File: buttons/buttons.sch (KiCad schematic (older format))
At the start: 20 parts, among them SW1 SW_Push, SW2 SW_Push, SW3 SW_Push, SW4 SW_Push, SW5 SW_Push, SW6 SW_Push, SW7 SW_Push, SW8 SW_Push

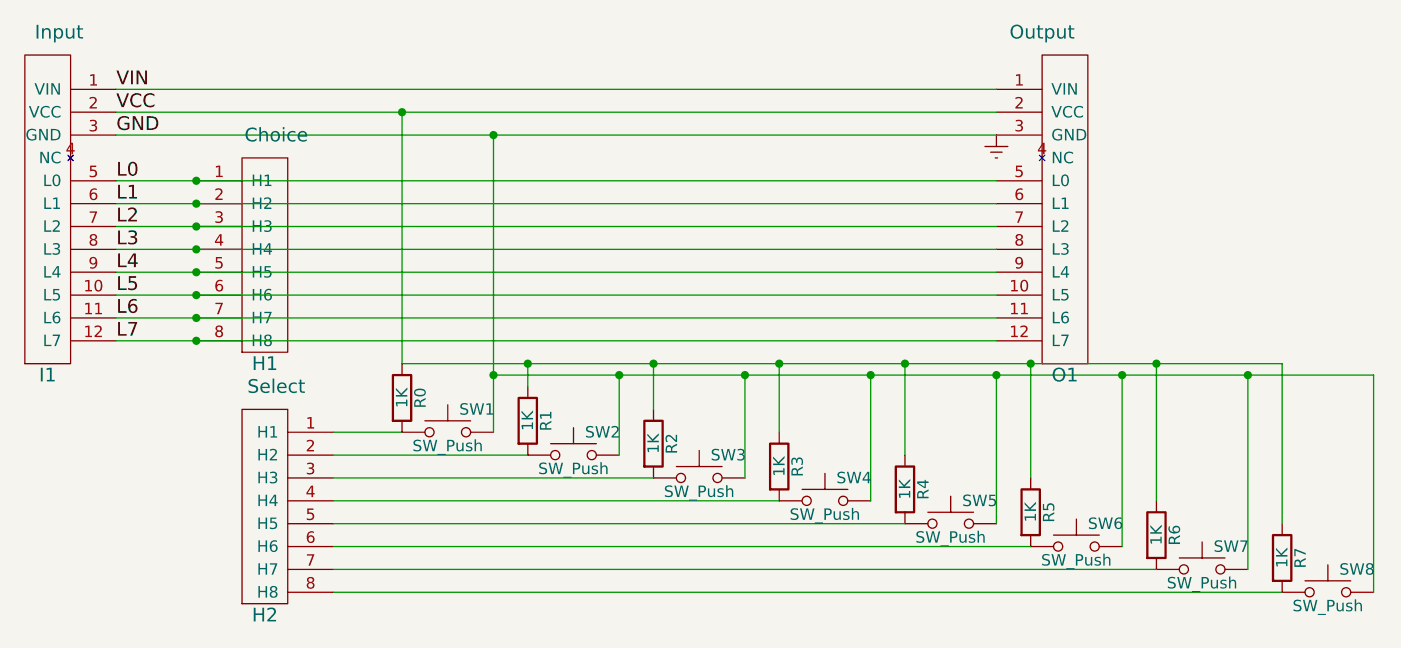
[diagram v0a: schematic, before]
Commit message: More work to ensure there are no errors from KiCAD's schematic checker. Fixed the multiplexer module, so that all 7 slaves will work (only 6 were working, due to a missing VCC to the "Next Output").
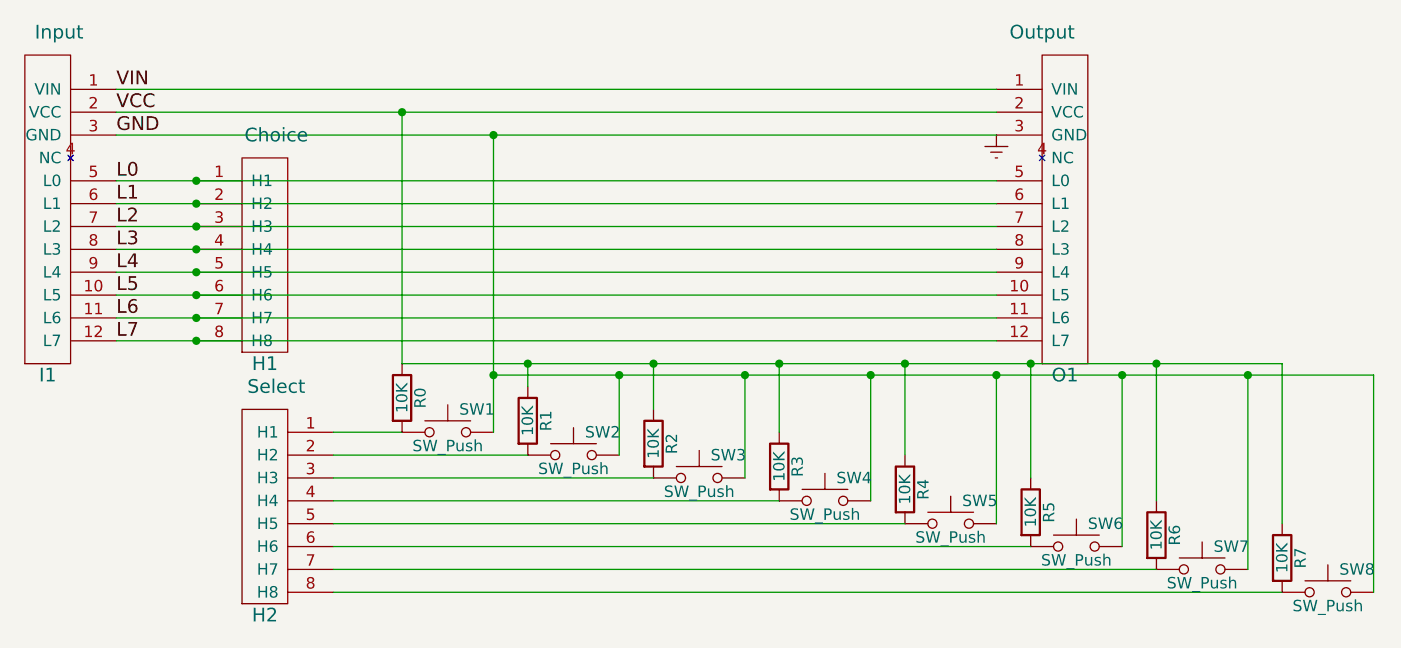
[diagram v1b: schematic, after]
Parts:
- R0, R1, R2, R3, R4, R5, R6, R7: value 1K -> 10K
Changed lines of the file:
@@
 LIBS:valves
 LIBS:eplay
-LIBS:Switch
-LIBS:buttons-cache
 EELAYER 25 0
 EELAYER END
@@
 P 3500 3250
 F 0 "R0" V 3580 3250 50  0000 C CNN
-F 1 "1K" V 3500 3250 50  0000 C CNN
+F 1 "10K" V 3500 3250 50  0000 C CNN
 F 2 "Resistors_THT:R_Axial_DIN0204_L3.6mm_D1.6mm_P7.62mm_Horizontal" V 3430 3250 50  0001 C CNN
 F 3 "" H 3500 3250 50  0001 C CNN
@@
 P 4050 3350
 F 0 "R1" V 4130 3350 50  0000 C CNN
-F 1 "1K" V 4050 3350 50  0000 C CNN
+F 1 "10K" V 4050 3350 50  0000 C CNN
 F 2 "Resistors_THT:R_Axial_DIN0204_L3.6mm_D1.6mm_P7.62mm_Horizontal" V 3980 3350 50  0001 C CNN
 F 3 "" H 4050 3350 50  0001 C CNN
@@
 P 4600 3450
 F 0 "R2" V 4680 3450 50  0000 C CNN
-F 1 "1K" V 4600 3450 50  0000 C CNN
+F 1 "10K" V 4600 3450 50  0000 C CNN
 F 2 "Resistors_THT:R_Axial_DIN0204_L3.6mm_D1.6mm_P7.62mm_Horizontal" V 4530 3450 50  0001 C CNN
 F 3 "" H 4600 3450 50  0001 C CNN
@@
 P 5150 3550
 F 0 "R3" V 5230 3550 50  0000 C CNN
-F 1 "1K" V 5150 3550 50  0000 C CNN
+F 1 "10K" V 5150 3550 50  0000 C CNN
 F 2 "Resistors_THT:R_Axial_DIN0204_L3.6mm_D1.6mm_P7.62mm_Horizontal" V 5080 3550 50  0001 C CNN
 F 3 "" H 5150 3550 50  0001 C CNN
@@
 P 5700 3650
 F 0 "R4" V 5780 3650 50  0000 C CNN
-F 1 "1K" V 5700 3650 50  0000 C CNN
+F 1 "10K" V 5700 3650 50  0000 C CNN
 F 2 "Resistors_THT:R_Axial_DIN0204_L3.6mm_D1.6mm_P7.62mm_Horizontal" V 5630 3650 50  0001 C CNN
 F 3 "" H 5700 3650 50  0001 C CNN
@@
 P 6250 3750
 F 0 "R5" V 6330 3750 50  0000 C CNN
-F 1 "1K" V 6250 3750 50  0000 C CNN
+F 1 "10K" V 6250 3750 50  0000 C CNN
 F 2 "Resistors_THT:R_Axial_DIN0204_L3.6mm_D1.6mm_P7.62mm_Horizontal" V 6180 3750 50  0001 C CNN
 F 3 "" H 6250 3750 50  0001 C CNN
@@
 P 6800 3850
 F 0 "R6" V 6880 3850 50  0000 C CNN
-F 1 "1K" V 6800 3850 50  0000 C CNN
+F 1 "10K" V 6800 3850 50  0000 C CNN
 F 2 "Resistors_THT:R_Axial_DIN0204_L3.6mm_D1.6mm_P7.62mm_Horizontal" V 6730 3850 50  0001 C CNN
 F 3 "" H 6800 3850 50  0001 C CNN
@@
 P 7350 3950
 F 0 "R7" V 7430 3950 50  0000 C CNN
-F 1 "1K" V 7350 3950 50  0000 C CNN
+F 1 "10K" V 7350 3950 50  0000 C CNN
 F 2 "Resistors_THT:R_Axial_DIN0204_L3.6mm_D1.6mm_P7.62mm_Horizontal" V 7280 3950 50  0001 C CNN
 F 3 "" H 7350 3950 50  0001 C CNN
